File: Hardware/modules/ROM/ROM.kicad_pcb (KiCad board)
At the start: 4 copper layers, 83.3 x 68.2 mm, 14 parts, among them J1 Bus_PCI_6502, U1 74HC138, U2 SST39SF040, U3 74HC00, U4 AS6C4008-55PCN

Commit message: Update Module Files and Readme
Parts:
- moved REF** 3.84 mm to (155.3, 98.4)
- moved REF** 3.84 mm to (176.9, 98.4)
- moved REF** 3.84 mm to (167.0, 98.4)
- moved G*** 3.84 mm to (143.1, 98.2)
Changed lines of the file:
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@@
 	(footprint "Symbol:WEEE-Logo_5.6x8mm_SilkScreen"
 		(layer "F.Cu")
-		(at 163.83 100.584)
+		(at 167.005 98.425)
 		(descr "Waste Electrical and Electronic Equipment Directive")
 		(tags "Logo WEEE")
@@
 	(footprint "Eigene:logo"
 		(layer "F.Cu")
-		(at 139.954 100.33)
+		(at 143.129 98.171)
 		(property "Reference" "G***"
 			(at 0 0 0)
@@
 	(footprint "Symbol:ESD-Logo_8.9x8mm_SilkScreen"
 		(layer "F.Cu")
-		(at 152.146 100.584)
+		(at 155.321 98.425)
 		(descr "Electrostatic discharge Logo")
 		(tags "Logo ESD")
@@
 	(footprint "Symbol:OSHW-Logo2_9.8x8mm_SilkScreen"
 		(layer "F.Cu")
-		(at 173.736 100.584)
+		(at 176.911 98.425)
 		(descr "Open Source Hardware Symbol")
 		(tags "Logo Symbol OSHW")
@@
 		(tags "PCI bus Edge Connector")
 		(property "Reference" "J1"
-			(at -11.81 5.78 180)
-			(layer "B.SilkS")
+			(at 24.125 5.78 -180)
+			(layer "F.SilkS")
 			(effects
 				(font
@@
 					(thickness 0.15)
 				)
-				(justify mirror)
 			)
 		)

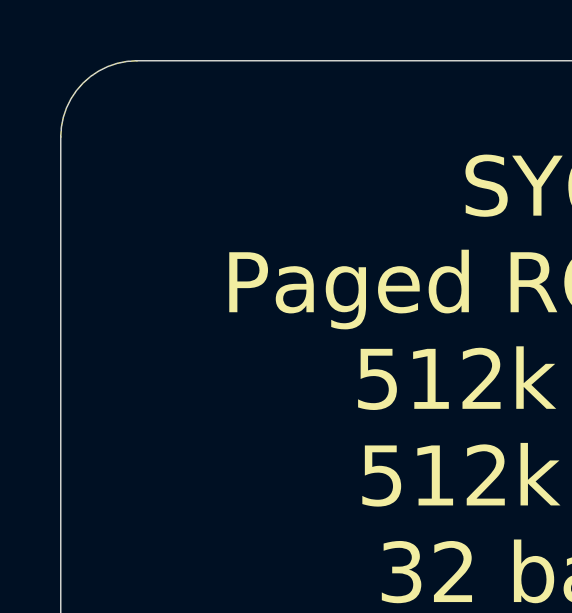
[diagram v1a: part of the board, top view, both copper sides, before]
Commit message: Hardware Update Add MyCPU VGA Module Beautify all Schematics minor Error corrections Readme Update
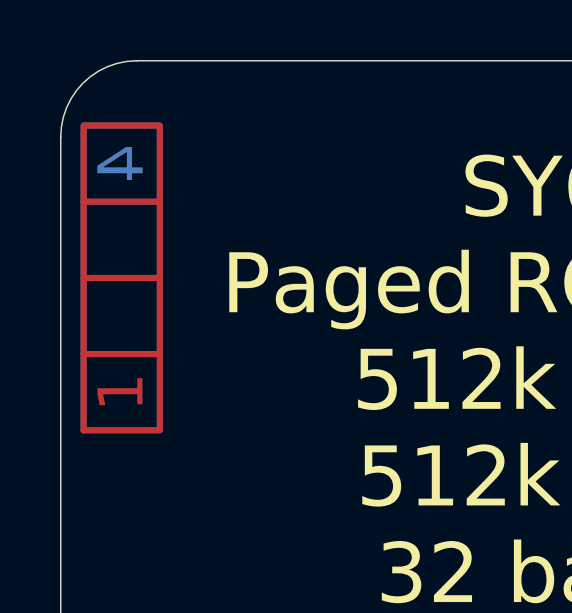
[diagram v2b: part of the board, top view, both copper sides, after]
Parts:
- added Ref**: Val**, Eigene:ladder_4, F.Cu at (120.9, 53.0)

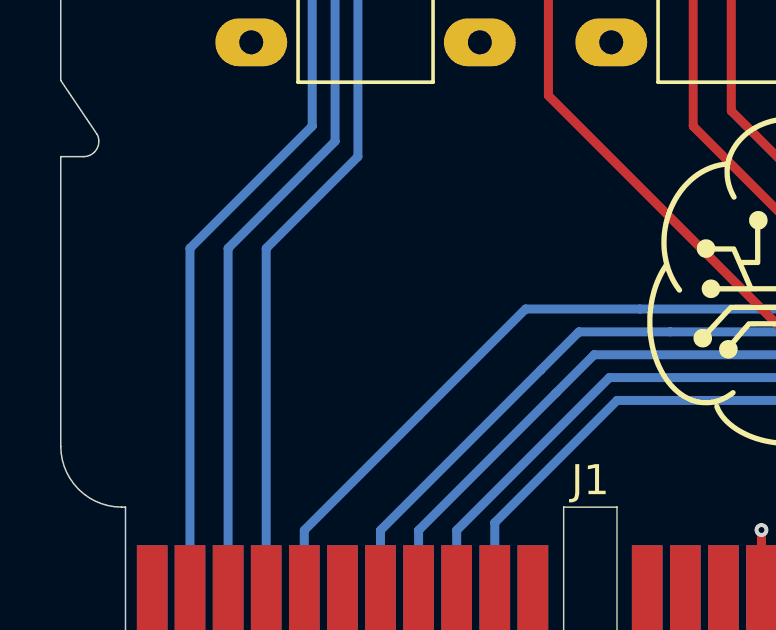
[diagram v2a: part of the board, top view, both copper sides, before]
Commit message: Hardware Review Pt. 1 fix Address Decoding for Strobe Generators add bulk capacitance to every board fix wiring of Prototyping Board
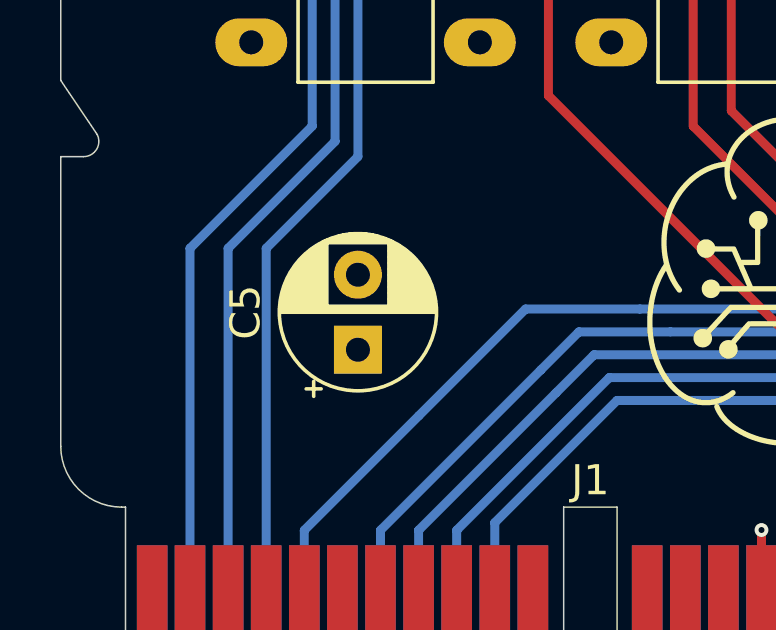
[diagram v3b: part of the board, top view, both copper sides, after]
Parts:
- added C5: 10µ, Capacitor_THT:CP_Radial_D5.0mm_P2.50mm, F.Cu at (128.8, 100.4)
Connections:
- J1 pad A12: /A15 -> unconnected-(J1-A15-PadA12)
- J1 pad A24: /~{IO} -> unconnected-(J1-~{IO}-PadA24)_0
- J1 pad A27: /~{IRQ_0.0} -> unconnected-(J1-~{IRQ_0.0}-PadA27)_0
- J1 pad A28: /~{IRQ_0.1} -> unconnected-(J1-~{IRQ_0.1}-PadA28)
- J1 pad A29: /~{IRQ_0.2} -> unconnected-(J1-~{IRQ_0.2}-PadA29)
- J1 pad A30: /~{IRQ_0.3} -> unconnected-(J1-~{IRQ_0.3}-PadA30)_0
- J1 pad A31: /~{IRQ_0.4} -> unconnected-(J1-~{IRQ_0.4}-PadA31)_0
- J1 pad A32: /~{IRQ_0.5} -> unconnected-(J1-~{IRQ_0.5}-PadA32)
- J1 pad A33: /~{IRQ_0.6} -> unconnected-(J1-~{IRQ_0.6}-PadA33)_0
- J1 pad A34: /~{IRQ_0.7} -> unconnected-(J1-~{IRQ_0.7}-PadA34)
- J1 pad A38: /SYNC_VPA -> unconnected-(J1-Sync/VPA-PadA38)
- J1 pad A39: /Ø2/VDA -> unconnected-(J1-Ø2/VDA-PadA39)
- J1 pad A41: /~{RDY} -> unconnected-(J1-~{RDY}-PadA41)
- J1 pad A42: /~{BE} -> unconnected-(J1-~{BE}-PadA42)_0
- J1 pad A45: /E -> unconnected-(J1-E-PadA45)_0
- J1 pad A53: /RAM_0 -> unconnected-(J1-RAM0-PadA53)_0
- J1 pad A54: /RAM_1 -> unconnected-(J1-RAM1-PadA54)
- J1 pad A55: /RAM_2 -> unconnected-(J1-RAM2-PadA55)_0
- J1 pad A56: /RAM_3 -> unconnected-(J1-RAM3-PadA56)
- J1 pad A58: /RAM_4 -> unconnected-(J1-RAM4-PadA58)
- J1 pad A59: /RAM_5 -> unconnected-(J1-RAM5-PadA59)_0
- J1 pad A60: /RAM_6 -> unconnected-(J1-RAM6-PadA60)
- J1 pad A61: /RAM_7 -> unconnected-(J1-RAM7-PadA61)
- J1 pad B12: /A14 -> unconnected-(J1-A14-PadB12)_0
- J1 pad B24: /~{L_RAM} -> unconnected-(J1-~{L_RAM}-PadB24)_0
- J1 pad B25: /~{H_RAM} -> unconnected-(J1-~{H_RAM}-PadB25)
- J1 pad B27: /~{IRQ} -> unconnected-(J1-~{IRQ}-PadB27)
- J1 pad B28: /~{IRQ_0} -> unconnected-(J1-~{IRQ_0}-PadB28)_0
- J1 pad B29: /~{IRQ_1} -> unconnected-(J1-~{IRQ_1}-PadB29)_0
- J1 pad B30: /~{IRQ_2} -> unconnected-(J1-~{IRQ_2}-PadB30)
- J1 pad B31: /~{IRQ_3} -> unconnected-(J1-~{IRQ_3}-PadB31)_0
- J1 pad B32: /~{IRQ_4} -> unconnected-(J1-~{IRQ_4}-PadB32)
- J1 pad B33: /~{NMI} -> unconnected-(J1-~{NMI}-PadB33)
- J1 pad B38: /~{VP} -> unconnected-(J1-~{VP}-PadB38)_0
- J1 pad B39: /~{ML} -> unconnected-(J1-~{ML}-PadB39)_0
- J1 pad B41: /~{RES} -> unconnected-(J1-~{RES}-PadB41)_0
- J1 pad B46: /M/X -> unconnected-(J1-M/~{X}-PadB46)_0

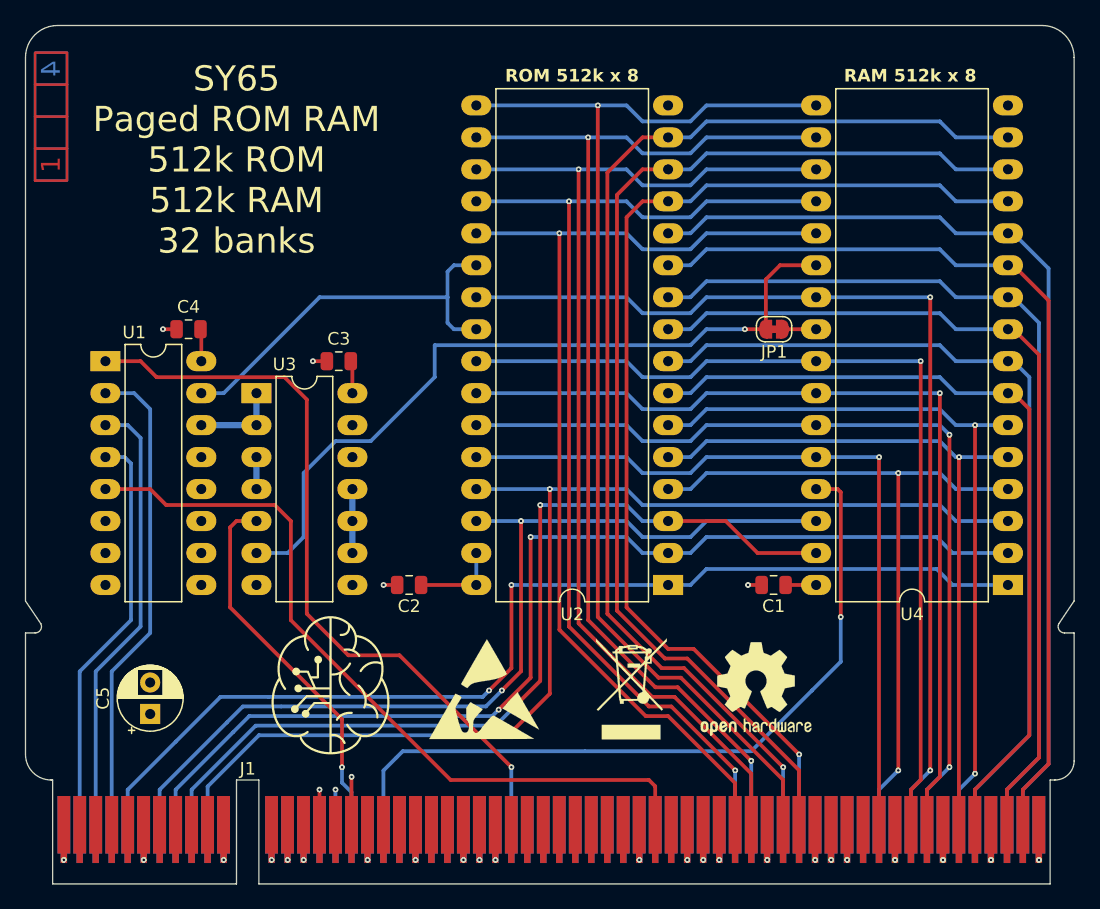
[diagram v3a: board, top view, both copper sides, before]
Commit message: Big Review Update - Changed Copper Pours on all PCBs - Implemented errors found at review - fixed some additional errors
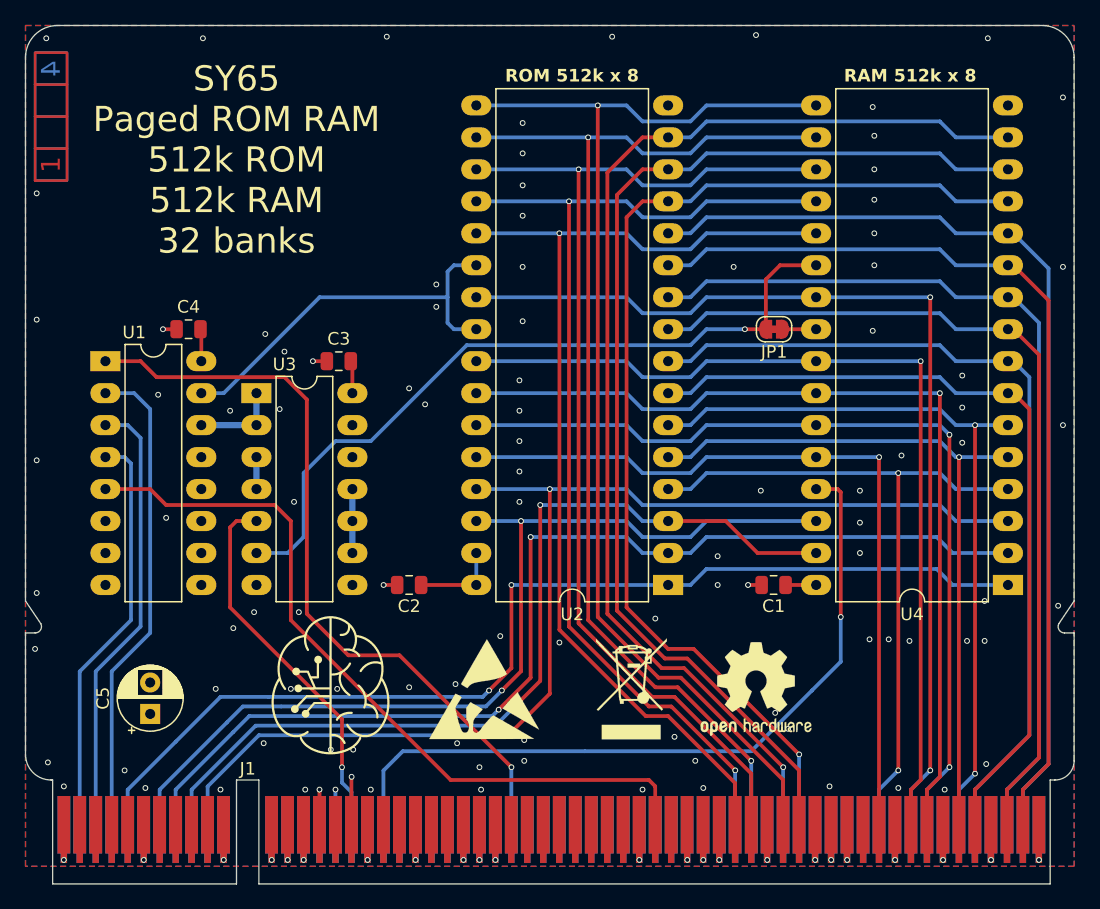
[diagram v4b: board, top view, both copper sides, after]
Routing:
- net Net-(JP1-B): track 60.7 -> 59.2 mm
- net +5V: vias 4 -> 101
- added copper zone on B.Cu, net +5V
- added copper zone on F.Cu, net +5V
- added copper zone on In1.Cu, net GND
- removed copper zone on In1.Cu, net +5V
